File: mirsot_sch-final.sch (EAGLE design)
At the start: 24 parts, among them IC1 7805DT

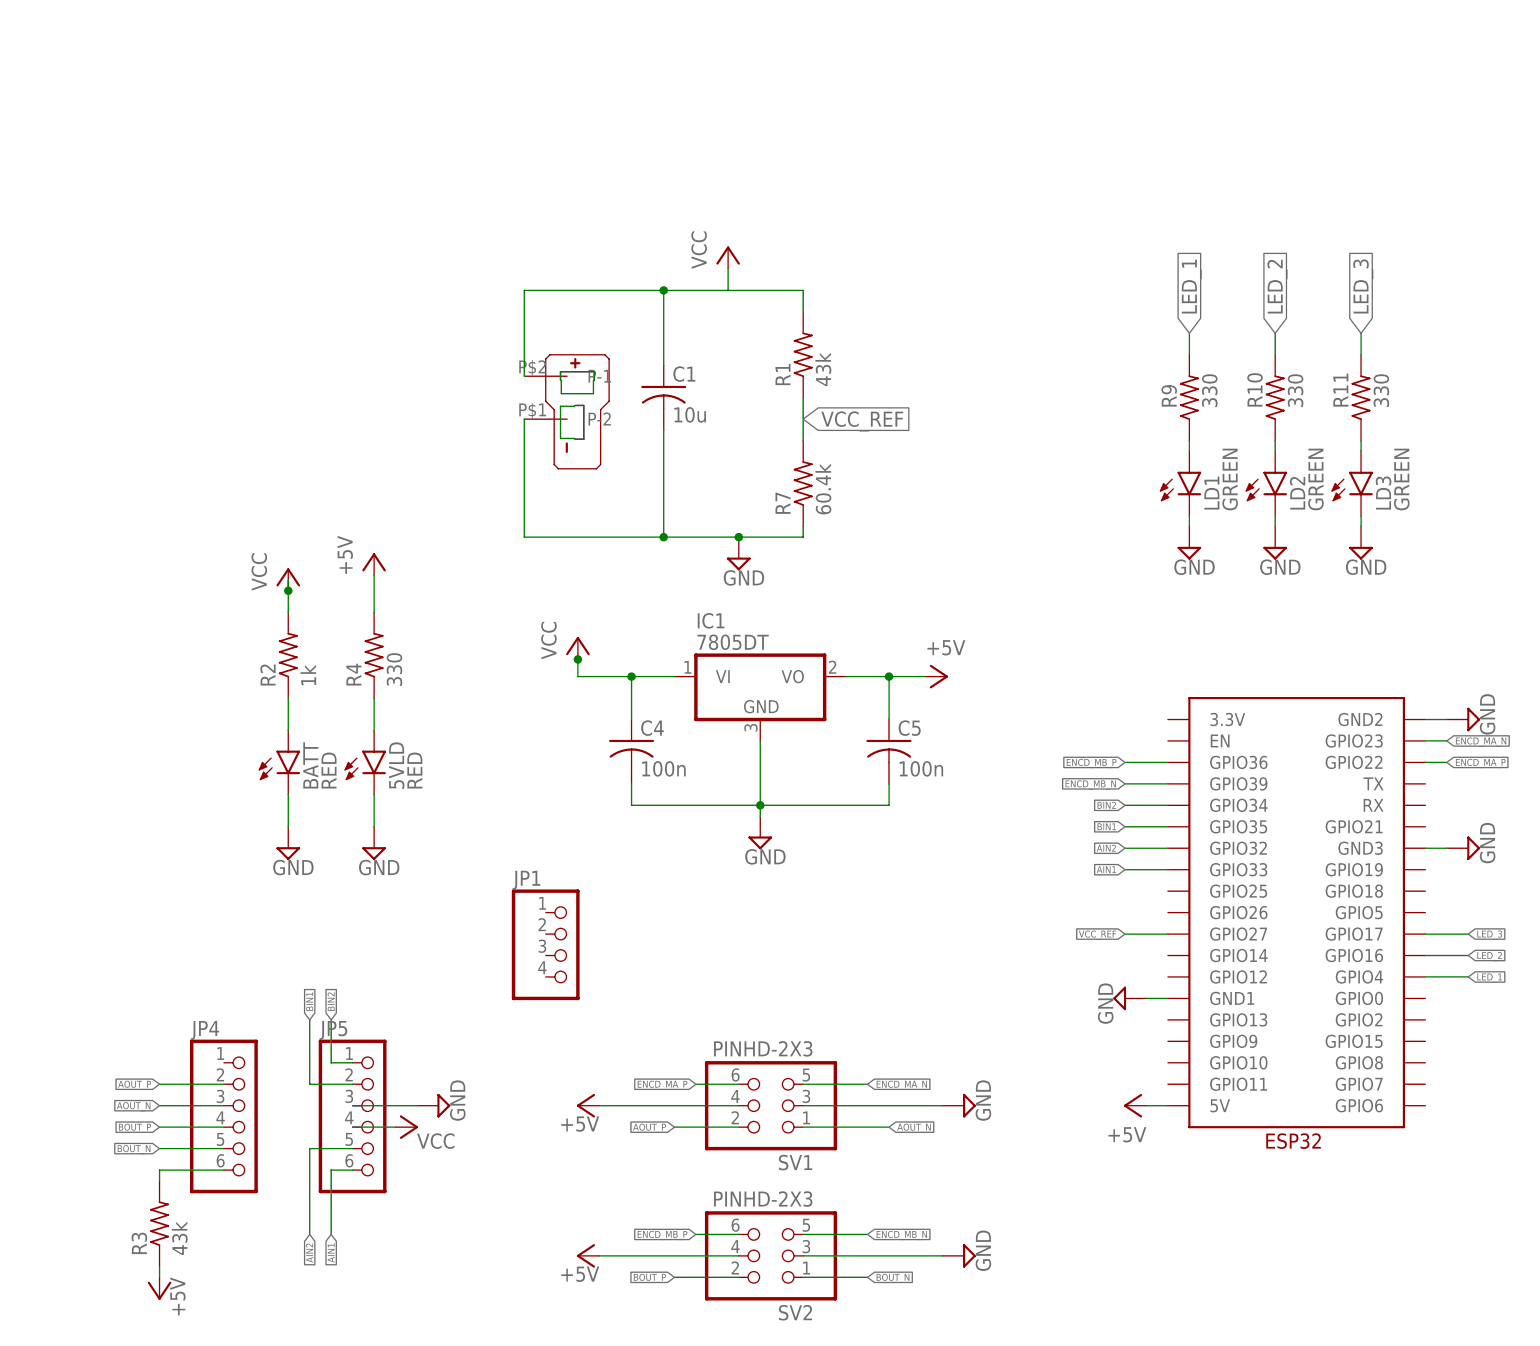
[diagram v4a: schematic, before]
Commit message: added level shifter, changed hole size, added switch
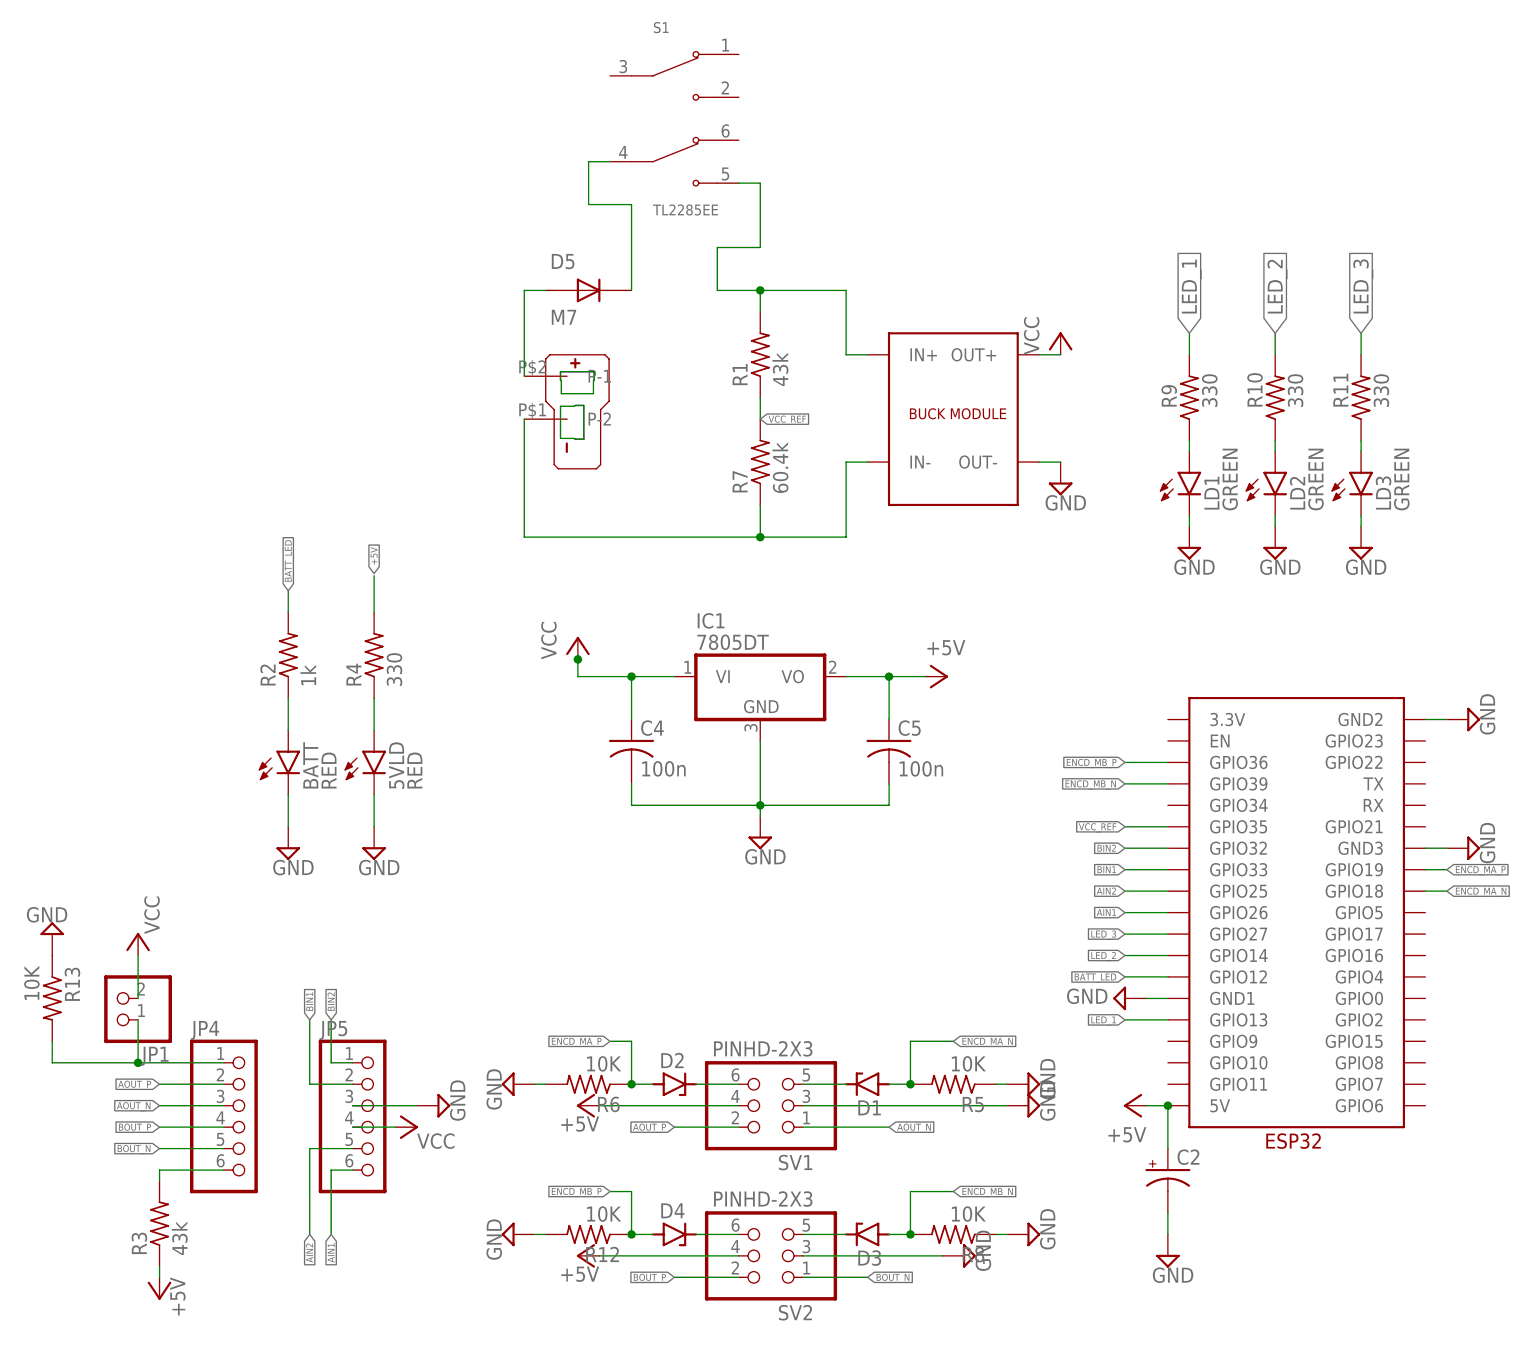
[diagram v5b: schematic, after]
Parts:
- removed C1: 10u, rcl:C-USC1206K
- added C2: (no value), rcl:CPOL-USE2.5-6
- added D1, D2, D3, D4: (no value), diode:ZENER-DIODEDO34-7
- added D5: M7, M7:M7
- added R12, R13, R5, R6, R8: 10K, rcl:R-US_M1206
- added S1: TL2285EE, TL2285EE:TL2285EE
- added U$3: BUCK_CONVERTER, BUCK_CONVERTER:BUCK_CONVERTER
- JP1: device pinhead:PINHD-1X4 -> pinhead:PINHD-1X2
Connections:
- new net BATT_LED: R2.2, U$2.GPIO12
- new net N$10: D4.C, SV2.6
- new net N$11: D5.A, U$1.P-1
- new net N$13: JP1.1, JP4.1, R13.2
- new net N$14: D5.C, S1.COM2
- new net N$15: R1.2, S1.NO2, U$3.IN+
- new net N$16: R7.1, U$1.P-2, U$3.IN-
- new net N$6: D1.C, SV1.5
- new net N$7: D2.C, SV1.6
- new net N$8: D3.C, SV2.5
- net +5V: now also C2.+
- net AIN1: now also U$2.GPIO26; no longer U$2.GPIO33
- net AIN2: now also U$2.GPIO25; no longer U$2.GPIO32
- net BIN1: now also U$2.GPIO33; no longer U$2.GPIO35
- net BIN2: now also U$2.GPIO32; no longer U$2.GPIO34
- net ENCD_MA_N: now also D1.A, R5.2, U$2.GPIO18; no longer SV1.5, U$2.GPIO23
- net ENCD_MA_P: now also D2.A, R6.1, U$2.GPIO19; no longer SV1.6, U$2.GPIO22
- net ENCD_MB_N: now also D3.A, R8.2; no longer SV2.5
- net ENCD_MB_P: now also D4.A, R12.1; no longer SV2.6
- net GND: now also C2.-, R12.2, R13.1, R5.1, R6.2, R8.1, U$3.OUT-; no longer C1.2, R7.1, U$1.P-2
- net LED_1: now also U$2.GPIO13; no longer U$2.GPIO4
- net LED_2: now also U$2.GPIO14; no longer U$2.GPIO16
- net LED_3: now also U$2.GPIO27; no longer U$2.GPIO17
- net VCC: now also JP1.2, U$3.OUT+; no longer C1.1, R1.2, R2.2, U$1.P-1
- net VCC_REF: now also U$2.GPIO35; no longer U$2.GPIO27
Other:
- moved on the sheet: R1, R7
